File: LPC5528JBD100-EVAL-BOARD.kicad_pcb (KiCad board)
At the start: 2 copper layers, 100 x 100 mm, 32 parts, among them J1 Jack-DC, J2 USB_B_Micro, U1 LM2596S-5, U2 LPC55S28JBD100, U3 LM1117-3.3, U4 LM1117-1.8, Y1 24MHz

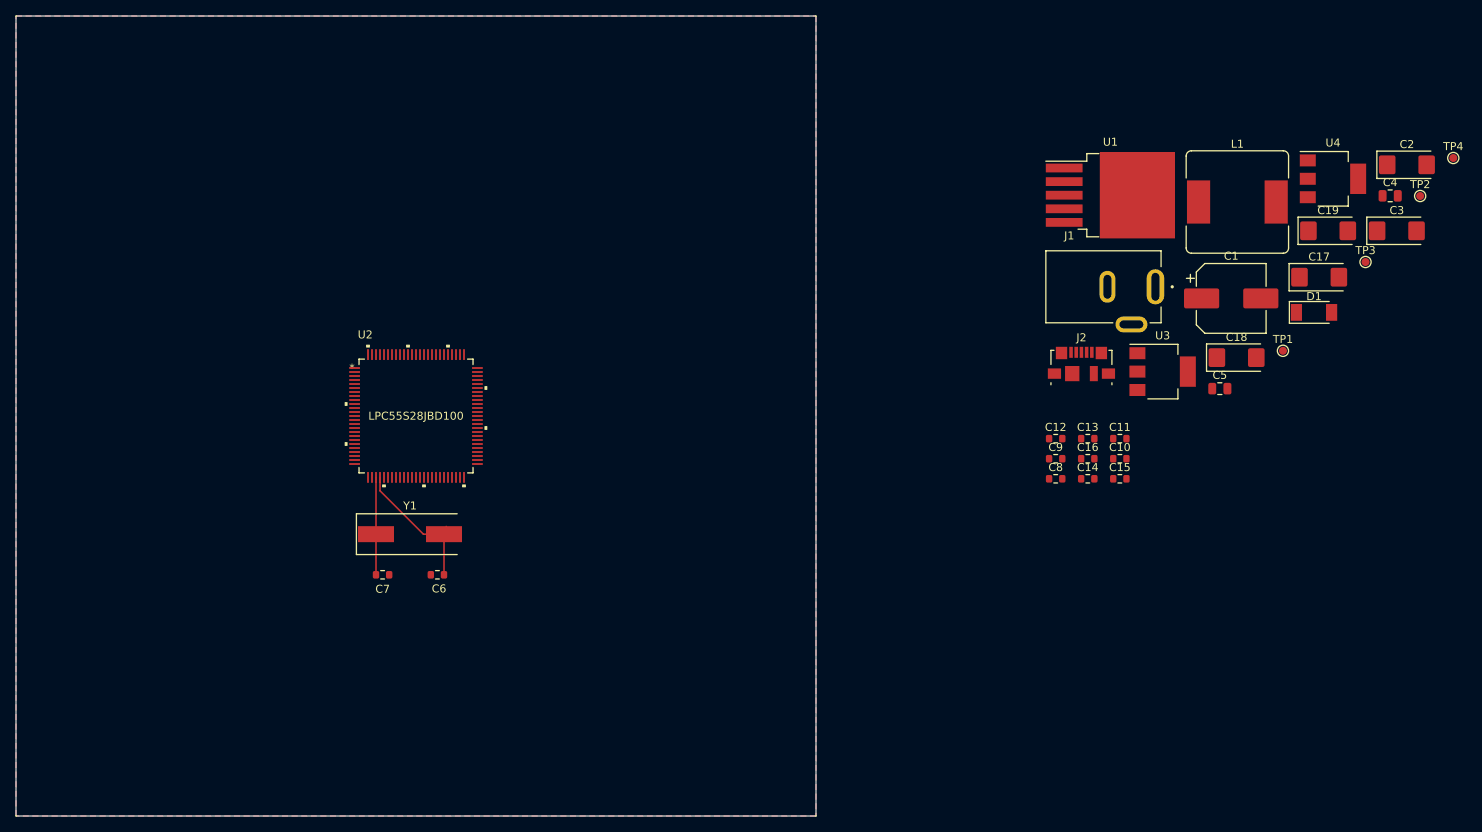
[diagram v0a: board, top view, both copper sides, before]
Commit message: LM2596 Layout oluşturuldu, USB Power switch tarafı eksik
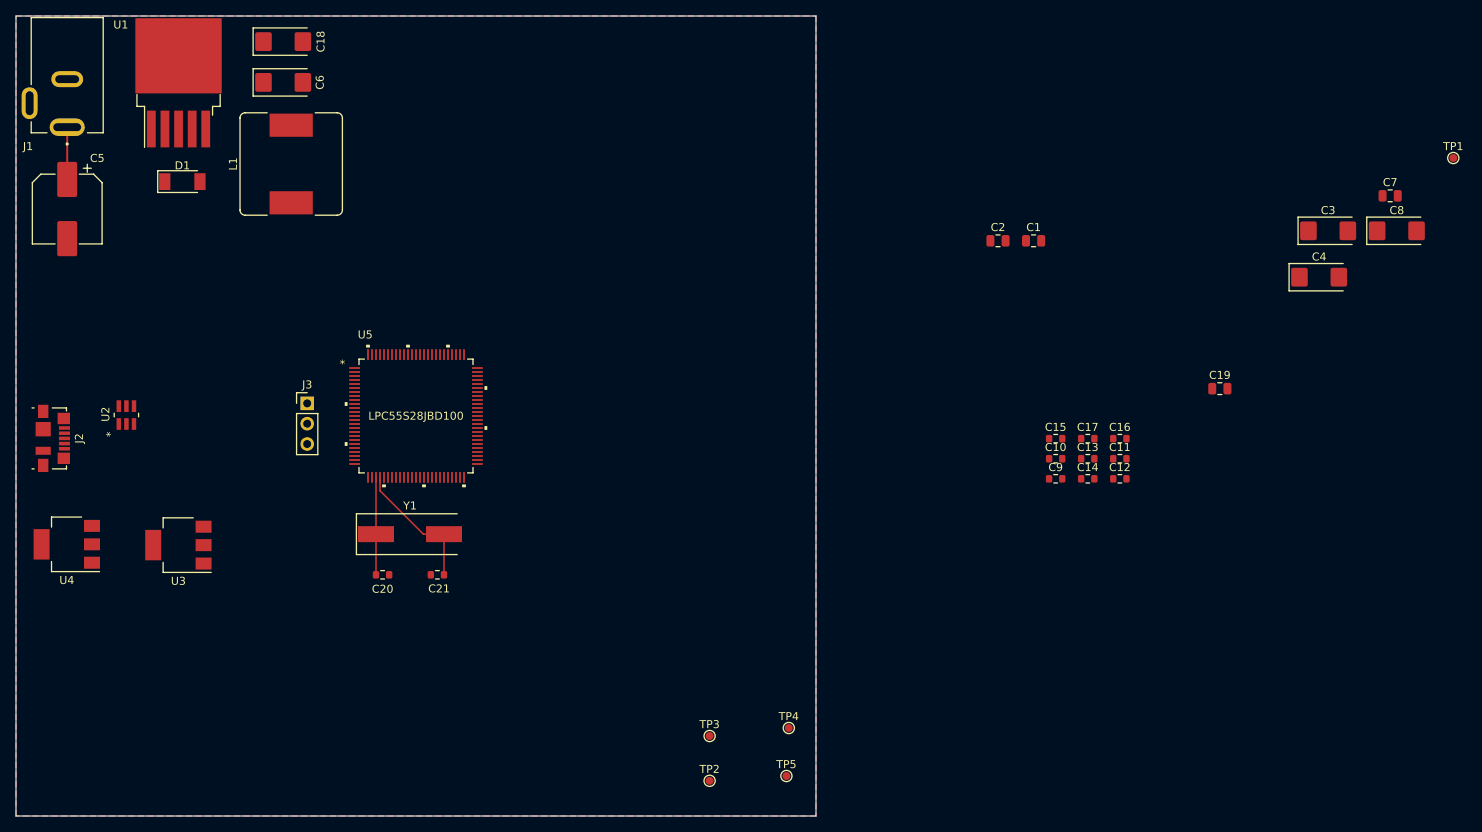
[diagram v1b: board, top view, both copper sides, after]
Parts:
- added C1: 4.7uF, Capacitor_SMD:C_0805_2012Metric, F.Cu at (127.2, 28.1)
- added C2: 4.7uF, Capacitor_SMD:C_0805_2012Metric, F.Cu at (122.8, 28.1)
- added J3: MCU_VOLTAGE_SEL, Connector_PinHeader_2.54mm:PinHeader_1x03_P2.54mm_Vertical, F.Cu at (36.4, 48.4)
- added TP5: TP_5V_EXT, TestPoint:TestPoint_Pad_D1.0mm, F.Cu at (96.3, 95.0)
- added U2: DBV6, erkan-hw-lib:TPS2552DBVR, F.Cu at (13.8, 49.9)
- moved U3 151.4 mm to (20.3, 66.1), turned to 180 degrees
- moved C5 145.9 mm to (6.40, 24.1), turned to -90 degrees
- moved D1 142.4 mm to (20.8, 20.7)
- moved C6 140.8 mm to (33.4, 8.30)
- moved U4 138.7 mm to (6.35, 66.0), turned to 180 degrees
- moved J1 132.6 mm to (6.40, 7.90), turned to -90 degrees
- moved J2 128.9 mm to (4.60, 52.8), turned to -90 degrees
- moved C18 125.6 mm to (33.4, 3.20)
- moved L1 118.4 mm to (34.4, 18.5), turned to 90 degrees
- moved U1 117.3 mm to (20.3, 8.35), turned to 90 degrees
- moved TP4 103.2 mm to (96.6, 89.0)
- moved TP3 101.2 mm to (86.7, 90.0)
- moved TP2 89.6 mm to (86.7, 95.6)
- renumbered C9 to C10, C10 to C11, C15 to C12, C16 to C13, C12 to C15, C11 to C16, C13 to C17, C5 to C19, C7 to C20, C6 to C21, C19 to C3, C17 to C4, C1 to C5, C2 to C6, C4 to C7, C3 to C8, C8 to C9, TP4 to TP1, TP1 to TP2, TP2 to TP4, U4 to U3, U3 to U4, U2 to U5
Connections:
- C18 pad 1: Net-(C18-Pad1) -> +5V
- C6 pad 1: Net-(C2-Pad1) -> +5V
- C7 pad 1: +5V -> 5V_EXT
- J2 pad 1: +5V -> VBUS
- U3 pad 3: Net-(C18-Pad1) -> +5V
- U4 pad 3: Net-(C2-Pad1) -> +5V
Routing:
- net V_IN: track 0.00 -> 7.14 mm
- net /MCU/MCU_XTAL32M_P: track 18.0 -> 17.0 mm
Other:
- rule pad_to_mask_clearance: 0 -> 0.05

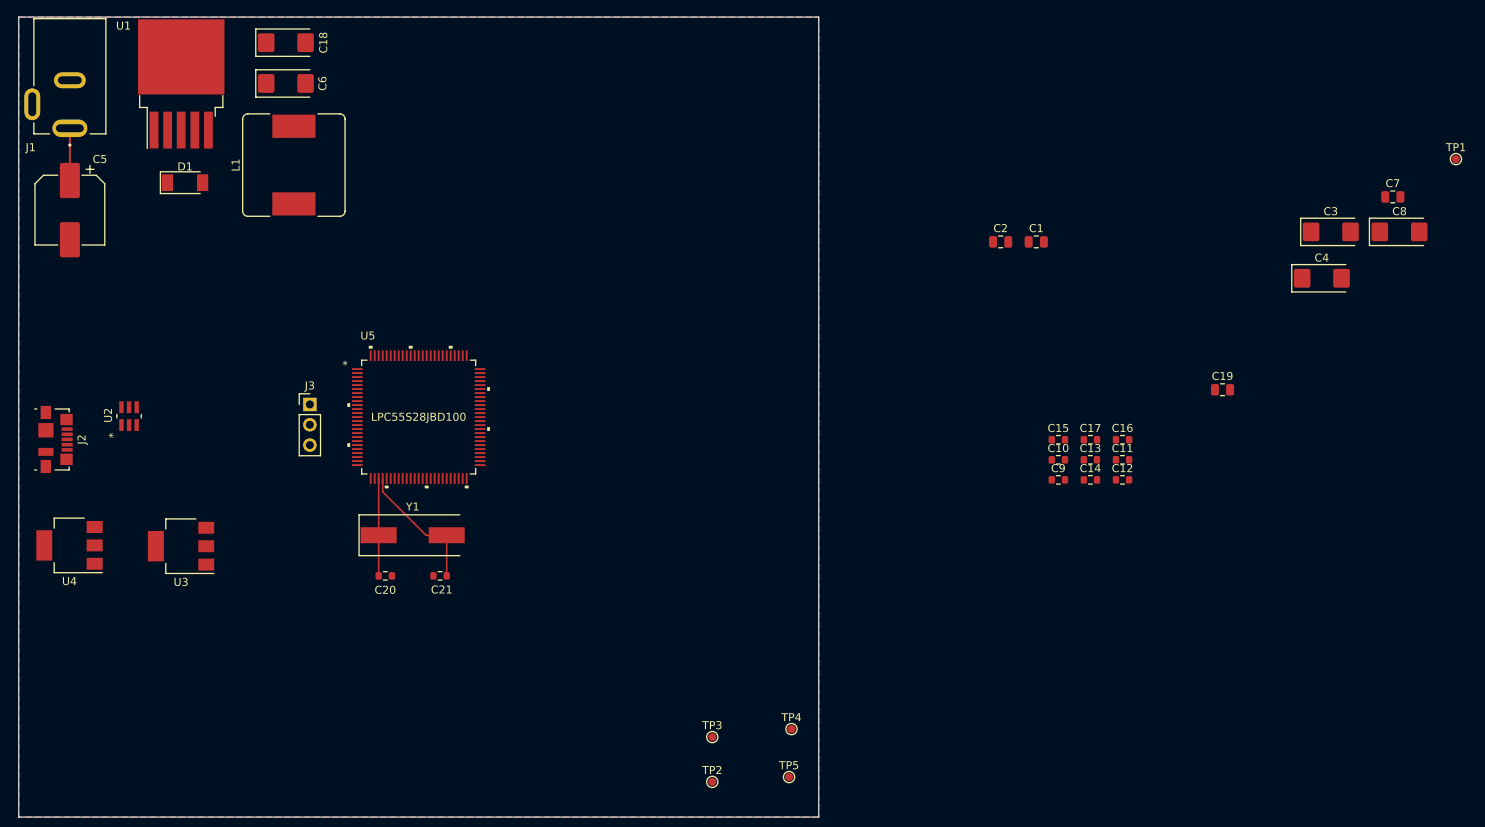
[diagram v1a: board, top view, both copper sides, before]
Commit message: LM2596 Layout ve yollar çizildi
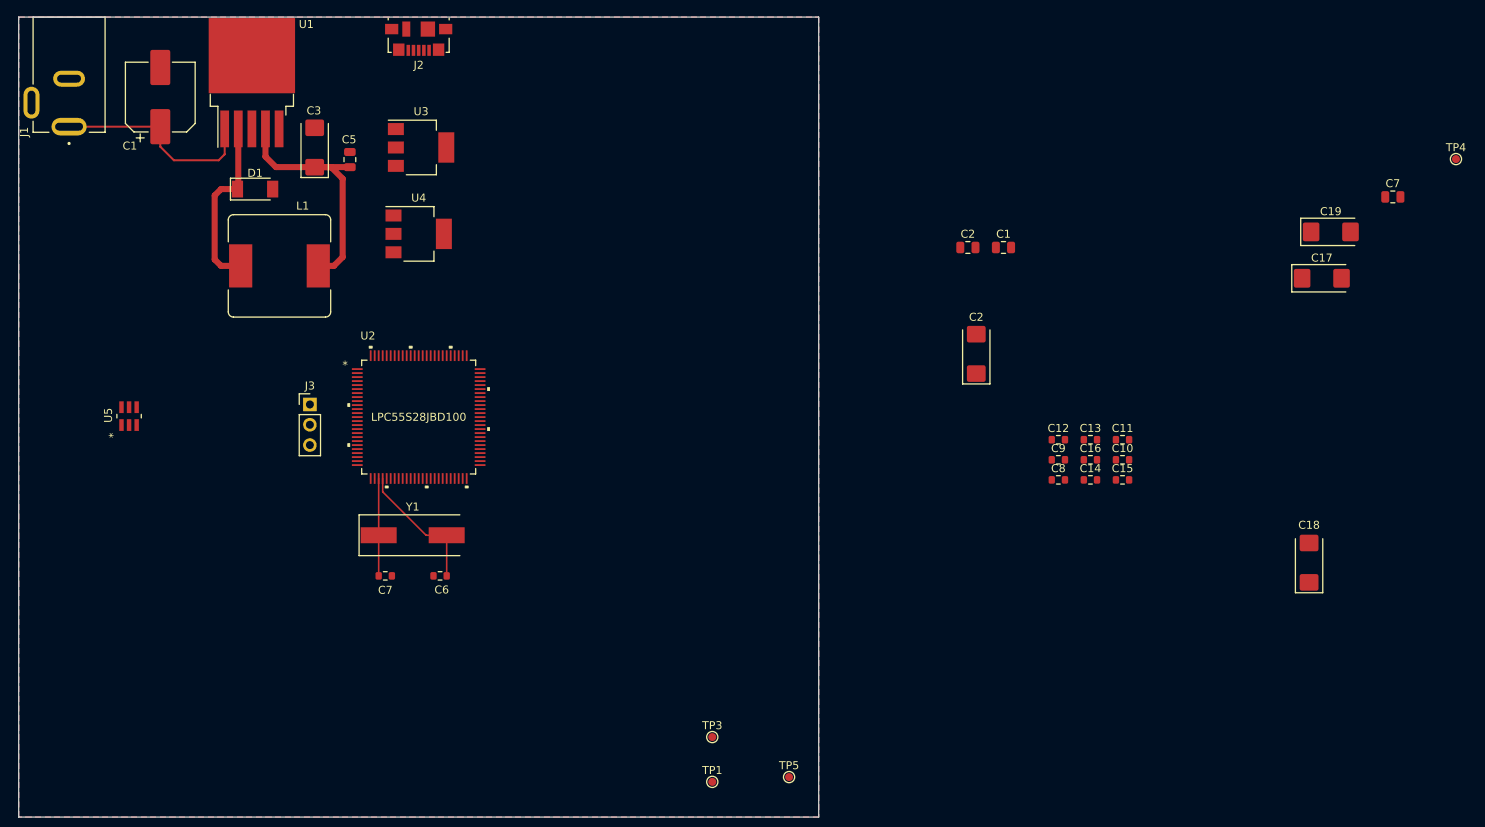
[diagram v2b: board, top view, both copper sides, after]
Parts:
- removed the TP4 at (96.6, 89.0)
- U5: renamed from U2; value DBV6 -> TPS2552DBVR
- moved C18 143.5 mm to (161.3, 68.2), turned to 90 degrees
- moved C3 136.0 mm to (37.0, 16.3), turned to 90 degrees
- moved C5 112.8 mm to (41.4, 17.8), turned to 90 degrees
- moved C2 92.7 mm to (119.7, 42.1), turned to 90 degrees
- moved J2 67.6 mm to (50.0, 2.70), turned to 180 degrees
- moved U3 66.4 mm to (50.3, 16.3), turned to 0 degrees
- moved U4 49.1 mm to (50.0, 27.1), turned to 0 degrees
- moved C1 18.1 mm to (17.7, 10.0), turned to 90 degrees
- moved L1 12.7 mm to (32.6, 31.1), turned to 0 degrees
- moved U1 8.83 mm to (29.1, 8.20)
- moved D1 8.79 mm to (29.6, 21.5)
- moved C1 4.16 mm to (123.1, 28.8)
- moved C2 4.16 mm to (118.7, 28.8)
- moved J1 0.22 mm to (6.30, 7.70)
- renumbered C5 to C1, C11 to C10, C16 to C11, C15 to C12, C17 to C13, C12 to C15, C13 to C16, C4 to C17, C3 to C19, C6 to C2, C8 to C3, C19 to C5, C21 to C6, C20 to C7, C9 to C8, C10 to C9, TP2 to TP1, TP1 to TP4, U5 to U2, U4 to U3, U3 to U4
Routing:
- net +5V: track 0.00 -> 30.8 mm
- net Net-(L1-Pad1): track 0.04 -> 20.4 mm
- net V_IN: track 7.14 -> 26.1 mm

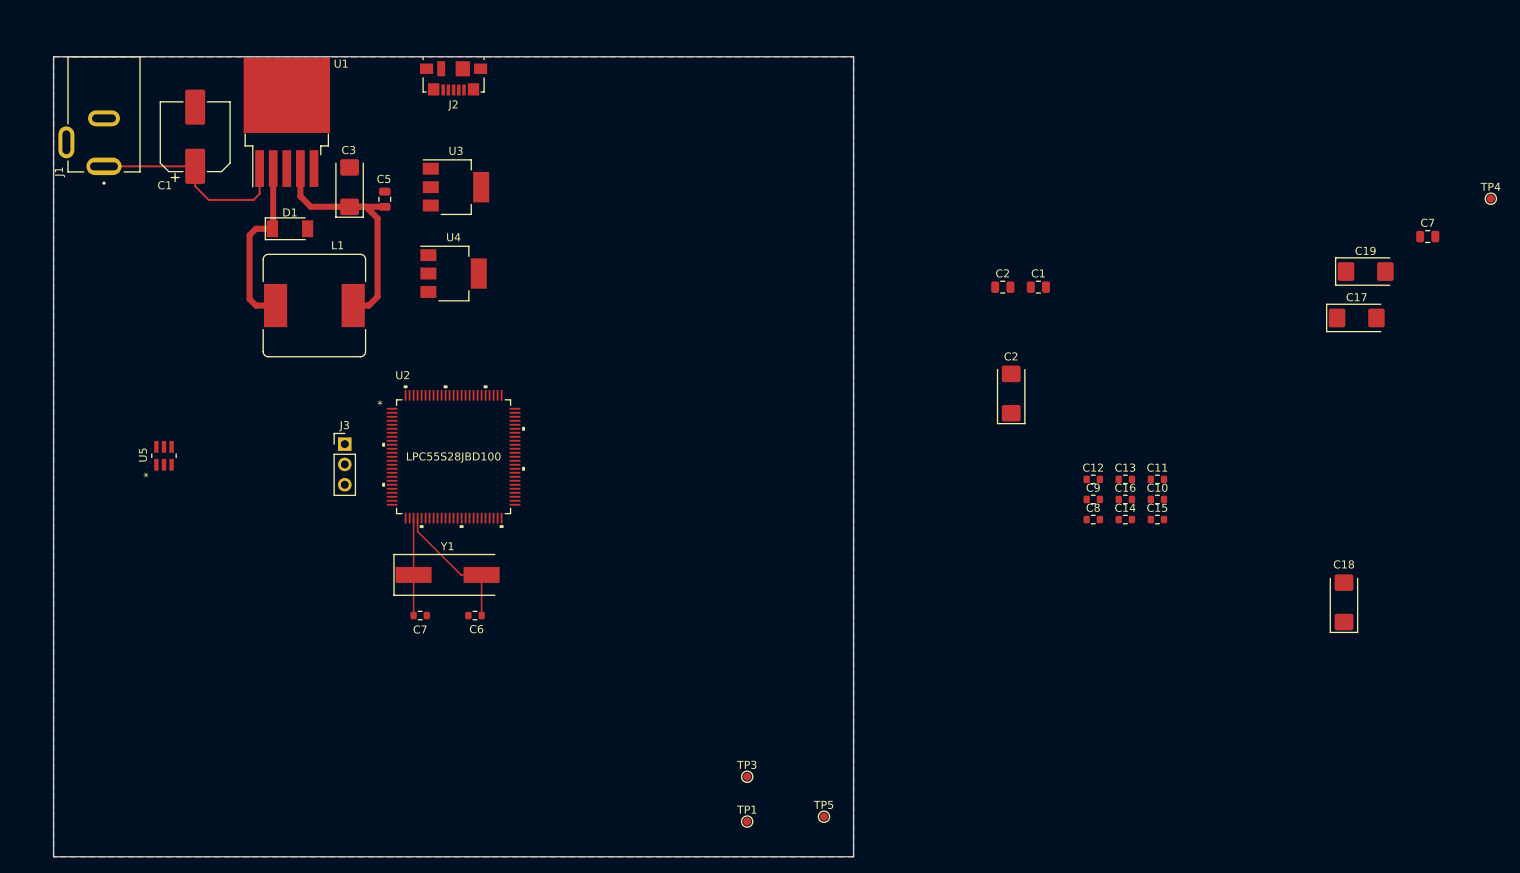
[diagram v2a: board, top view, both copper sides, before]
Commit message: LM2596 layout değiştirildi
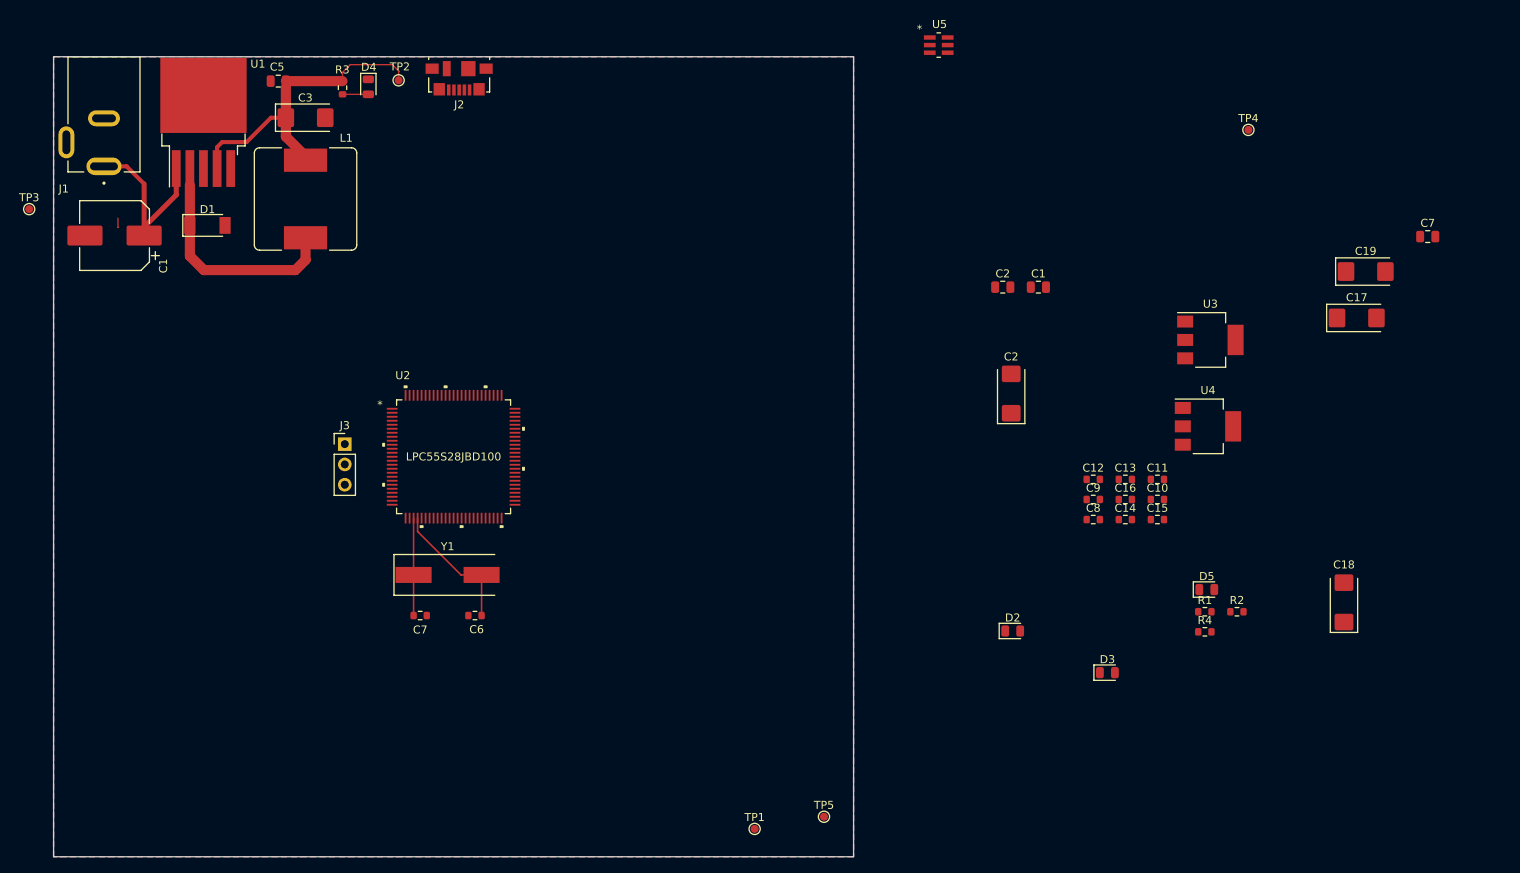
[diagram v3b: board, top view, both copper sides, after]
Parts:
- added D2: LED, LED_SMD:LED_0805_2012Metric, F.Cu at (119.9, 71.8)
- added D3: LED, LED_SMD:LED_0805_2012Metric, F.Cu at (131.7, 77.0)
- added D4: LED, LED_SMD:LED_0805_2012Metric, F.Cu at (39.3, 3.76)
- added D5: LED, LED_SMD:LED_0805_2012Metric, F.Cu at (144.2, 66.6)
- added R1: 0 Ohm, Resistor_SMD:R_0603_1608Metric, F.Cu at (143.9, 69.4)
- added R2: 1.2k Ohm, Resistor_SMD:R_0603_1608Metric, F.Cu at (147.9, 69.4)
- added R3: 220 Ohm, Resistor_SMD:R_0603_1608Metric, F.Cu at (36.1, 3.87)
- added R4: 68 Ohm, Resistor_SMD:R_0603_1608Metric, F.Cu at (143.9, 71.9)
- added TP2: TP_5V, TestPoint:TestPoint_Pad_D1.0mm, F.Cu at (43.1, 2.95)
- moved TP3 114.4 mm to (-3.05, 19.1)
- moved U5 109.6 mm to (110.6, -1.46), turned to 0 degrees
- moved U4 96.2 mm to (144.3, 46.2)
- moved U3 96.2 mm to (144.6, 35.4)
- moved TP4 31.5 mm to (149.4, 9.14)
- moved C5 19.9 mm to (28.1, 3.05), turned to 180 degrees
- moved C1 15.9 mm to (7.62, 22.4), turned to 180 degrees
- moved L1 13.4 mm to (31.5, 17.8), turned to 90 degrees
- moved U1 10.4 mm to (18.7, 8.20)
- moved D1 10.3 mm to (19.2, 21.1)
- moved C3 10.3 mm to (31.5, 7.62), turned to 0 degrees
- moved TP1 1.31 mm to (87.6, 96.5)
- moved J2 0.70 mm to (50.7, 2.69)
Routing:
- net Net-(D1-Pad1): track 20.4 -> 29.4 mm
- net +5V: track 30.8 -> 37.8 mm
- net V_IN: track 26.1 -> 22.4 mm
- net Net-(D4-Pad2): track 0.00 -> 3.23 mm
- net (no net): track 0.00 -> 1.24 mm
